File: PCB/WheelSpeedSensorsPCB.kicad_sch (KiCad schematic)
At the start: 21 parts, among them J1 RearLeftWheel, J10 FrontRightShock, J11 RearRightShock, J2 FrontRightWheel, J3 RearRightWheel, J4 Conn_01x02_Pin, J5 FrontLeftWheel, J6 RearLeftShock, J7 VehicleBus, J8 Conn_01x02_Pin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

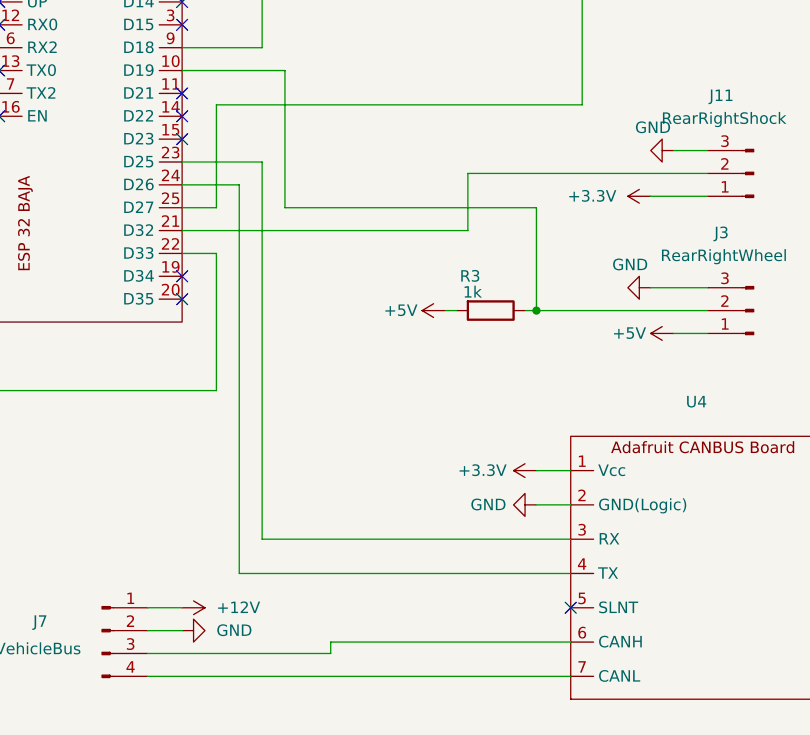
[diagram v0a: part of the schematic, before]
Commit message: Fix schematic/PCB to use proper CAN TX and RX pins
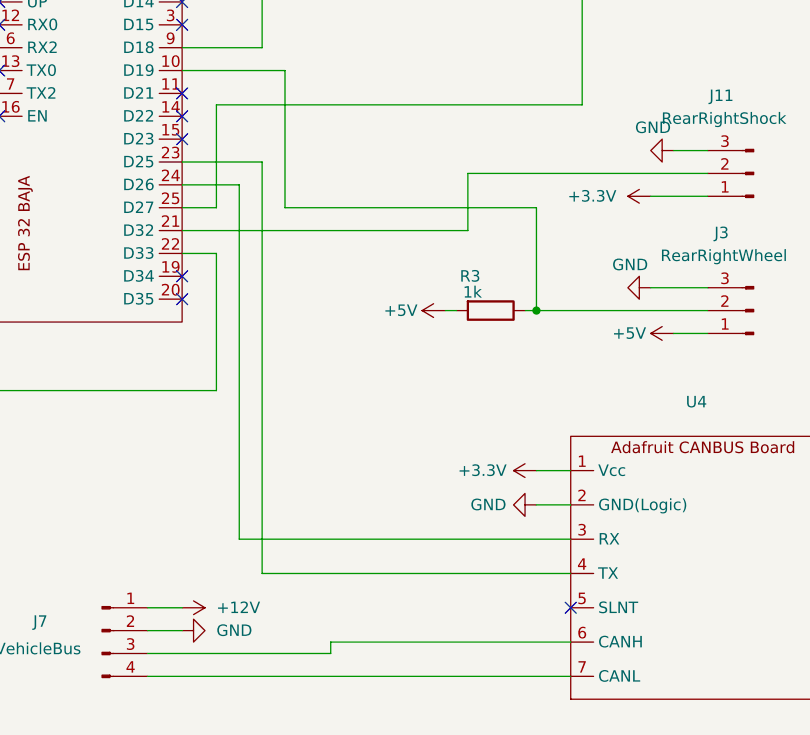
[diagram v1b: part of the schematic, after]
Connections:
- net at U3.23 (D25): now also U4.4 (TX); no longer U4.3 (RX)
- net at U3.24 (D26): now also U4.3 (RX); no longer U4.4 (TX)
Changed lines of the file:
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@@
+	(wire
+		(pts
+			(xy 119.38 135.89) (xy 156.21 135.89)
+		)
+		(stroke
+			(width 0)
+			(type default)
+		)
+	)
 	(wire
 		(pts
@@
 	(wire
 		(pts
-			(xy 119.38 139.7) (xy 119.38 96.52)
-		)
-		(stroke
-			(width 0)
-			(type default)
-		)
-	)
-	(wire
-		(pts
 			(xy 119.38 34.29) (xy 121.92 34.29)
 		)
@@
 	(wire
 		(pts
-			(xy 121.92 135.89) (xy 156.21 135.89)
-		)
-		(stroke
-			(width 0)
-			(type default)
-		)
-	)
-	(wire
-		(pts
 			(xy 116.84 99.06) (xy 116.84 87.63)
 		)
@@
 	(wire
 		(pts
+			(xy 119.38 135.89) (xy 119.38 96.52)
+		)
+		(stroke
+			(width 0)
+			(type default)
+		)
+	)
+	(wire
+		(pts
 			(xy 113.03 101.6) (xy 144.78 101.6)
 		)
@@
 	(wire
 		(pts
+			(xy 156.21 139.7) (xy 121.92 139.7)
+		)
+		(stroke
+			(width 0)
+			(type default)
+		)
+	)
+	(wire
+		(pts
 			(xy 146.05 52.07) (xy 152.4 52.07)
 		)
@@
 	(wire
 		(pts
-			(xy 156.21 139.7) (xy 119.38 139.7)
-		)
-		(stroke
-			(width 0)
-			(type default)
-		)
-	)
-	(wire
-		(pts
 			(xy 90.17 34.29) (xy 86.36 34.29)
 		)
@@
 	(wire
 		(pts
-			(xy 121.92 93.98) (xy 121.92 135.89)
-		)
-		(stroke
+			(xy 121.92 93.98) (xy 121.92 139.7)
+		)
+		(stroke
